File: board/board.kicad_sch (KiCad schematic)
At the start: 0 parts

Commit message: Adding 'THE BUTTON'
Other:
- added sheet The Button (button.kicad_sch)
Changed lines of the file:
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@@
 	(generator_version "8.0")
 	(paper "A4")
+	(sheet
+		(at 20.32 21.59)
+		(size 12.7 20.32)
+		(fields_autoplaced yes)
+		(stroke
+			(width 0.1524)
+			(type solid)
+		)
+		(fill
+			(color 0 0 0 0.0000)
+		)
+		(property "Sheetname" "The Button"
+			(at 20.32 20.8784 0)
+			(effects
+				(font
+					(size 1.27 1.27)
+				)
+				(justify left bottom)
+			)
+		)
+		(property "Sheetfile" "button.kicad_sch"
+			(at 20.32 42.4946 0)
+			(effects
+				(font
+					(size 1.27 1.27)
+				)
+				(justify left top)
+			)
+		)
+		(pin "GND" input
+			(at 33.02 39.37 0)
+			(effects
+				(font
+					(size 1.27 1.27)
+				)
+				(justify right)
+			)
+		)
+		(pin "SDA" bidirectional
+			(at 33.02 35.56 0)
+			(effects
+				(font
+					(size 1.27 1.27)
+				)
+				(justify right)
+			)
+		)
+		(pin "~{INT}" output
+			(at 33.02 31.75 0)
+			(effects
+				(font
+					(size 1.27 1.27)
+				)
+				(justify right)
+			)
+		)
+		(pin "SCL" bidirectional
+			(at 33.02 27.94 0)
+			(effects
+				(font
+					(size 1.27 1.27)
+				)
+				(justify right)
+			)
+		)
+		(pin "VCC" input
+			(at 33.02 24.13 0)
+			(effects
+				(font
+					(size 1.27 1.27)
+				)
+				(justify right)
+			)
+		)
+		(instances
+			(project "board"
+				(path "/b5a6c315-00b5-445d-a49f-bfda9e5399e4"
+					(page "2")
+				)
+			)
+		)
+	)
 	(sheet_instances
 		(path "/"

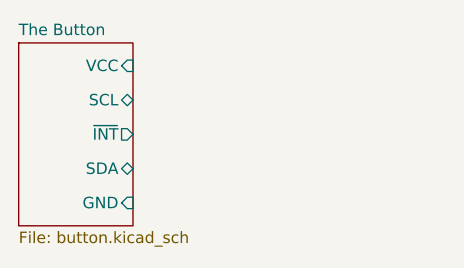
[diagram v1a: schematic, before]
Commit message: Creating PCB for 'THE BUTTON'
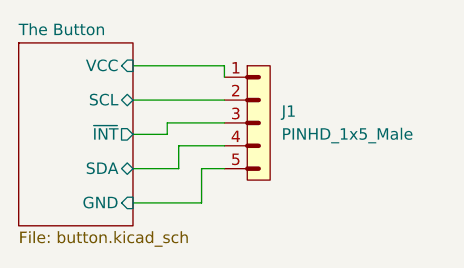
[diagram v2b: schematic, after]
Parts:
- added J1: PINHD_1x5_Male, Connector_PinHeader_2.54mm:PinHeader_1x05_P2.54mm_Horizontal, symbol PCM_SL_Pin_Headers:PINHD_1x5_Male
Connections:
- net The Button/GND: now also J1.5
- net The Button/SCL: now also J1.2
- net The Button/SDA: now also J1.4
- net The Button/VCC: now also J1.1
- net The Button/~{INT}: now also J1.3
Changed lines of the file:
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@@
 	(generator_version "8.0")
 	(paper "A4")
+	(wire
+		(pts
+			(xy 40.64 39.37) (xy 40.64 35.56)
+		)
+		(stroke
+			(width 0)
+			(type default)
+		)
+	)
+	(wire
+		(pts
+			(xy 43.18 24.13) (xy 43.18 25.4)
+		)
+		(stroke
+			(width 0)
+			(type default)
+		)
+	)
+	(wire
+		(pts
+			(xy 36.83 31.75) (xy 36.83 30.48)
+		)
+		(stroke
+			(width 0)
+			(type default)
+		)
+	)
+	(wire
+		(pts
+			(xy 33.02 31.75) (xy 36.83 31.75)
+		)
+		(stroke
+			(width 0)
+			(type default)
+		)
+	)
+	(wire
+		(pts
+			(xy 33.02 24.13) (xy 43.18 24.13)
+		)
+		(stroke
+			(width 0)
+			(type default)
+		)
+	)
+	(wire
+		(pts
+			(xy 33.02 27.94) (xy 43.18 27.94)
+		)
+		(stroke
+			(width 0)
+			(type default)
+		)
+	)
+	(wire
+		(pts
+			(xy 38.1 35.56) (xy 38.1 33.02)
+		)
+		(stroke
+			(width 0)
+			(type default)
+		)
+	)
+	(wire
+		(pts
+			(xy 33.02 39.37) (xy 40.64 39.37)
+		)
+		(stroke
+			(width 0)
+			(type default)
+		)
+	)
+	(wire
+		(pts
+			(xy 33.02 35.56) (xy 38.1 35.56)
+		)
+		(stroke
+			(width 0)
+			(type default)
+		)
+	)
+	(wire
+		(pts
+			(xy 36.83 30.48) (xy 43.18 30.48)
+		)
+		(stroke
+			(width 0)
+			(type default)
+		)
+	)
+	(wire
+		(pts
+			(xy 38.1 33.02) (xy 43.18 33.02)
+		)
+		(stroke
+			(width 0)
+			(type default)
+		)
+	)
+	(wire
+		(pts
+			(xy 40.64 35.56) (xy 43.18 35.56)
+		)
+		(stroke
+			(width 0)
+			(type default)
+		)
+	)
+	(symbol
+		(lib_id "PCM_SL_Pin_Headers:PINHD_1x5_Male")
+		(at 46.99 30.48 0)
+		(unit 1)
+		(exclude_from_sim no)
+		(in_bom yes)
+		(on_board yes)
+		(dnp no)
+		(fields_autoplaced yes)
+		(property "Reference" "J1"
+			(at 49.53 29.2099 0)
+			(effects
+				(font
+					(size 1.27 1.27)
+				)
+				(justify left)
+			)
+		)
+		(property "Value" "PINHD_1x5_Male"
+			(at 49.53 31.7499 0)
+			(effects
+				(font
+					(size 1.27 1.27)
+				)
+				(justify left)
+			)
+		)
+		(property "Footprint" "Connector_PinHeader_2.54mm:PinHeader_1x05_P2.54mm_Horizontal"
+			(at 45.72 17.78 0)
+			(effects
+				(font
+					(size 1.27 1.27)
+				)
+				(hide yes)
+			)
+		)
+		(property "Datasheet" ""
+			(at 46.99 19.05 0)
+			(effects
+				(font
+					(size 1.27 1.27)
+				)
+				(hide yes)
+			)
+		)
+		(property "Description" "Pin Header male with pin space 2.54mm. Pin Count -5"
+			(at 46.99 30.48 0)
+			(effects
+				(font
+					(size 1.27 1.27)
+				)
+				(hide yes)
+			)
+		)
+		(pin "3"
+		)
+		(pin "1"
+		)
+		(pin "4"
+		)
+		(pin "5"
+		)
+		(pin "2"
+		)
+		(instances
+			(project "board"
+				(path "/b5a6c315-00b5-445d-a49f-bfda9e5399e4"
+					(reference "J1")
+					(unit 1)
+				)
+			)
+		)
+	)
 	(sheet
 		(at 20.32 21.59)
